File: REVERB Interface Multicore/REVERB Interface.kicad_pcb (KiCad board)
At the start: 2 copper layers, 90.2 x 95.9 mm, 59 parts, among them J1 RPiZeroW, J2 Iridium, J3 APRS, J4 Antenna, J5 UPDI, M1 MountingHole_Pad, M2 MountingHole_Pad, M3 MountingHole_Pad, M4 MountingHole_Pad, M5 PiMount, M6 PiMount, M7 PiMount, M8 PiMount, U1 LSM9DS1BOB, U2 MAX3232, U3 ATtiny1604-SS, U4 TXB0104D

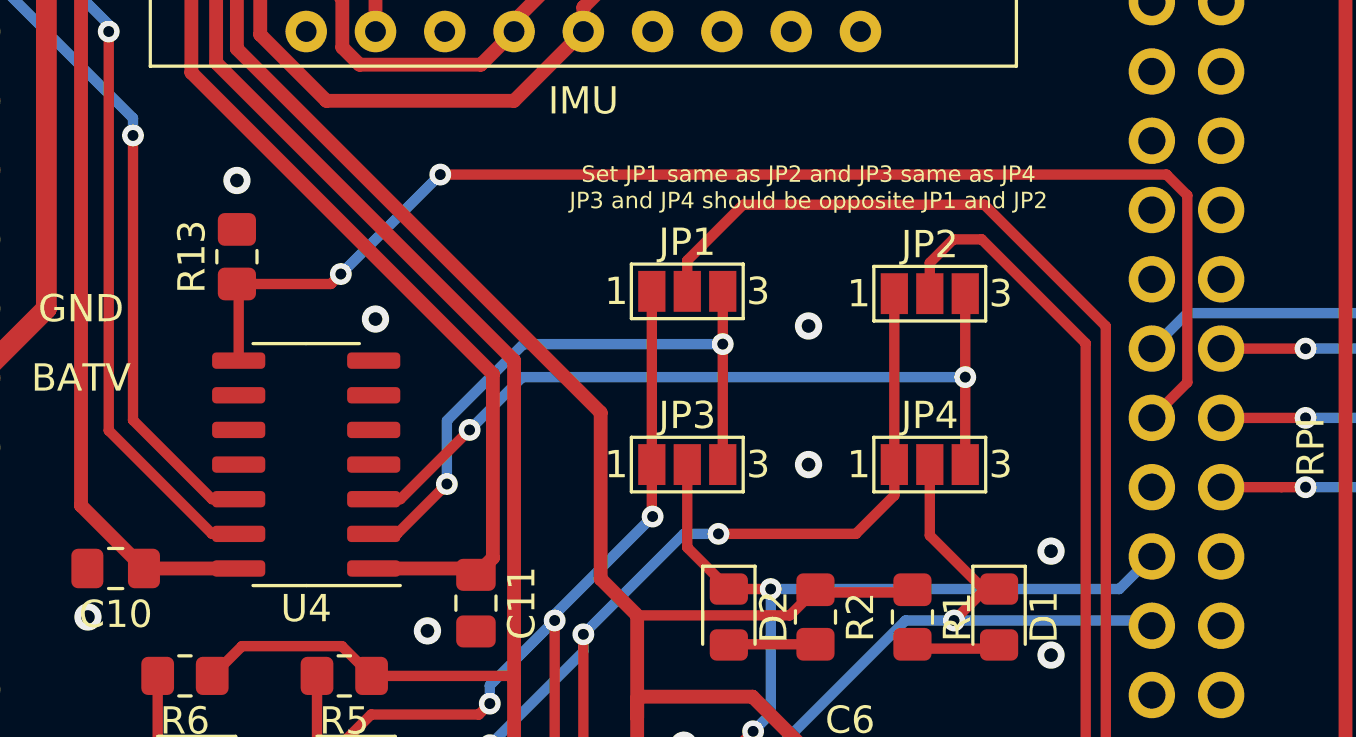
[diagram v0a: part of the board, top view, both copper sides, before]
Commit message: tie OE high
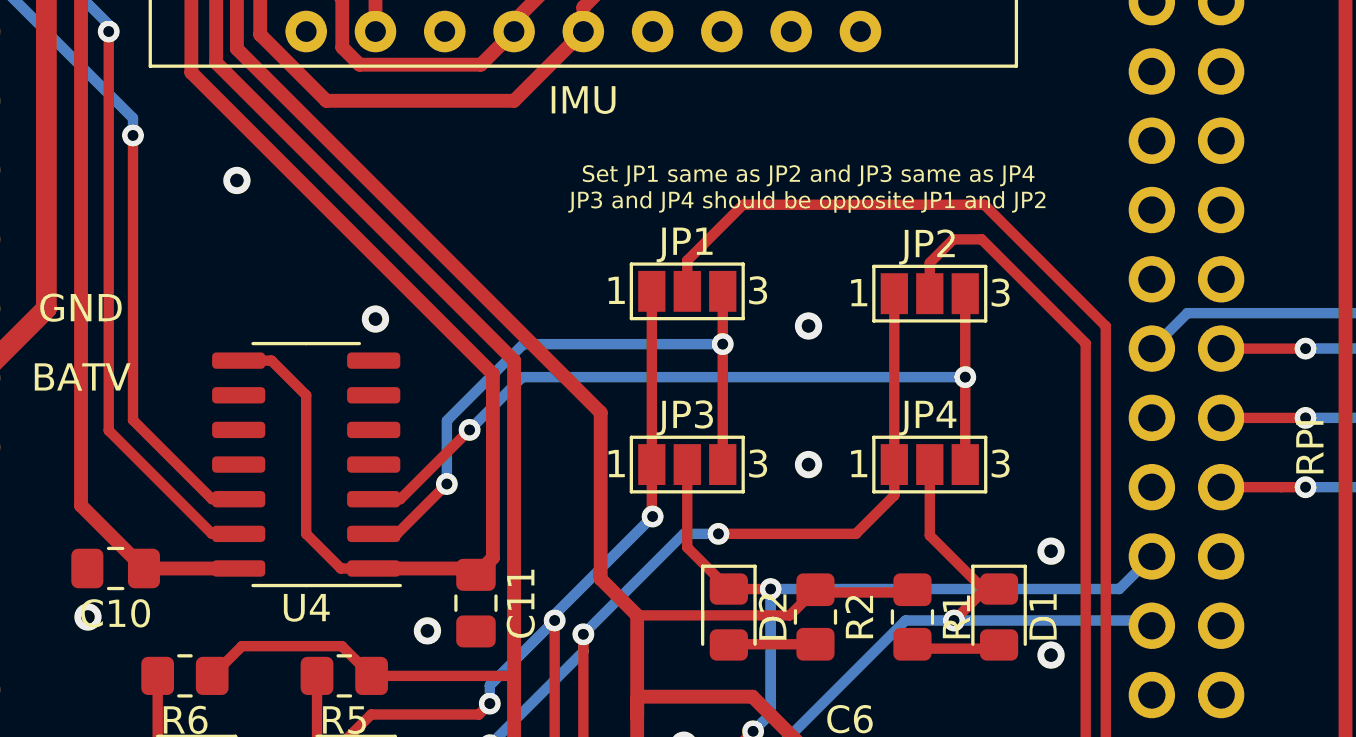
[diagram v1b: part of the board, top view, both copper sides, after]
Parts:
- removed R13: 10K, Resistor_SMD:R_0805_2012Metric_Pad1.20x1.40mm_HandSolder
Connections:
- J1 pad 22: /OE -> (no net)
- U4 pad 8: /OE -> +3V3
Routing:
- net /OE: track 48.3 -> 0.00 mm, vias 2 -> 0
- net +3V3: track 83.4 -> 94.5 mm

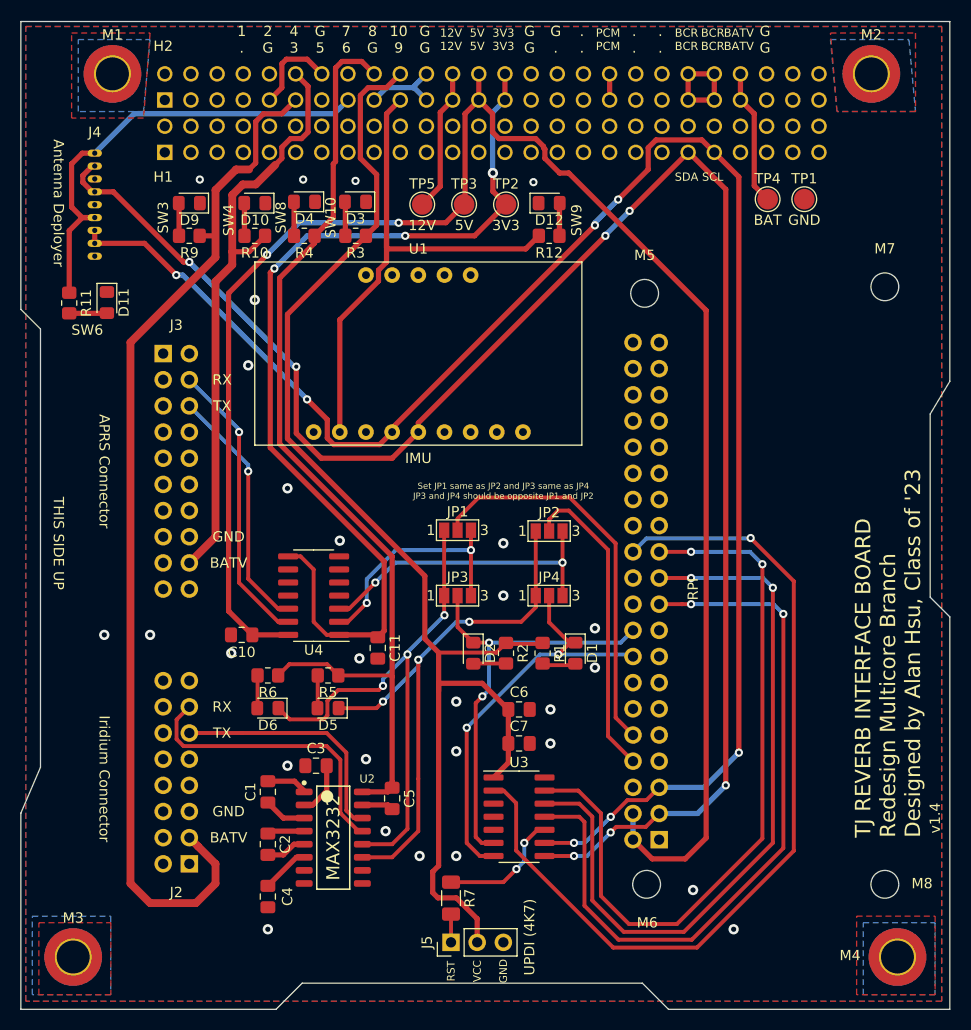
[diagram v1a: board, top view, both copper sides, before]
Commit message: Add decoupling
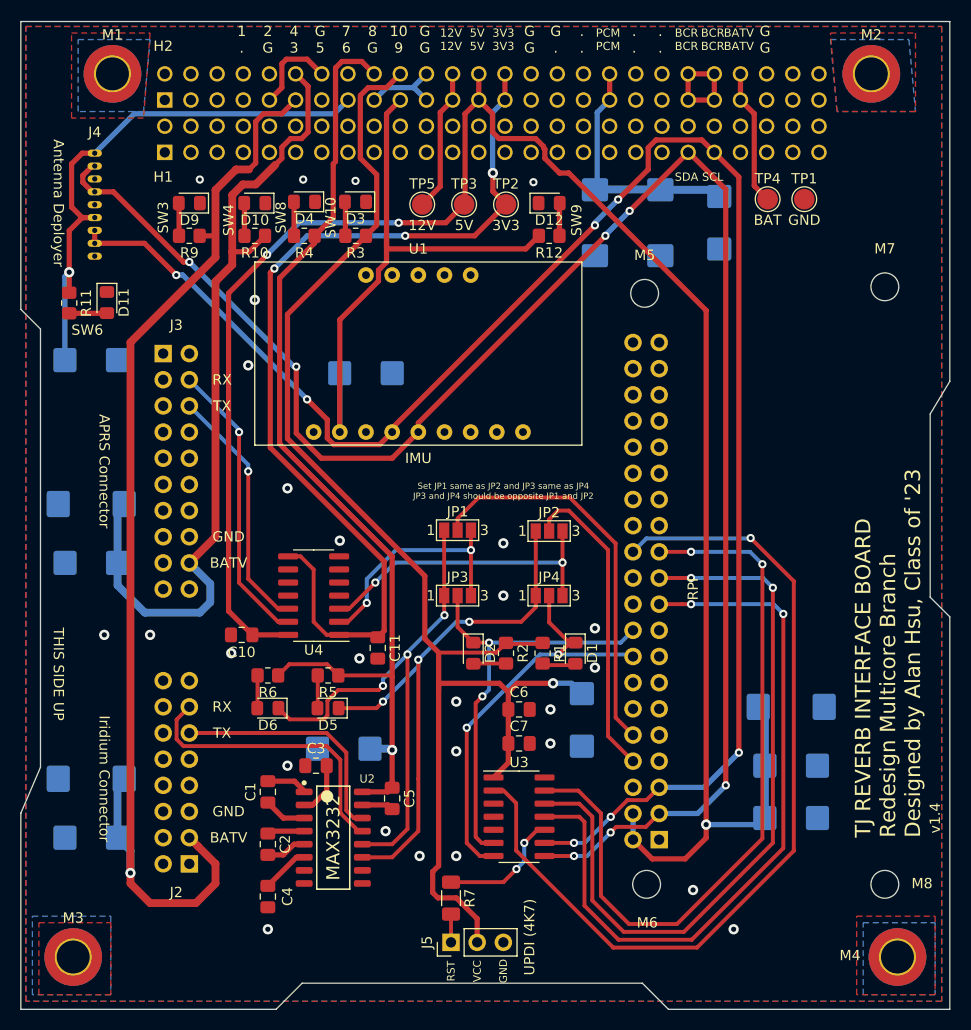
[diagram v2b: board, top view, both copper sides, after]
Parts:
- added C12: 22uF, Capacitor_Tantalum_SMD:CP_EIA-6032-28_Kemet-C_Pad2.25x2.35mm_HandSolder, B.Cu at (181.6, 130.2)
- added C13: 100uF, Capacitor_Tantalum_SMD:CP_EIA-7343-43_Kemet-X_Pad2.25x2.55mm_HandSolder, B.Cu at (113.7, 126.4)
- added C14: 47uF, Capacitor_Tantalum_SMD:CP_EIA-6032-28_Kemet-C_Pad2.25x2.35mm_HandSolder, B.Cu at (113.7, 132.1)
- added C15: 47uF, Capacitor_Tantalum_SMD:CP_EIA-6032-28_Kemet-C_Pad2.25x2.35mm_HandSolder, B.Cu at (113.7, 85.7)
- added C16: 47uF, Capacitor_Tantalum_SMD:CP_EIA-6032-28_Kemet-C_Pad2.25x2.35mm_HandSolder, B.Cu at (140.3, 87.0)
- added C17: 100uF, Capacitor_Tantalum_SMD:CP_EIA-7343-43_Kemet-X_Pad2.25x2.55mm_HandSolder, B.Cu at (162.6, 72.4)
- added C18: 100uF, Capacitor_Tantalum_SMD:CP_EIA-7343-43_Kemet-X_Pad2.25x2.55mm_HandSolder, B.Cu at (168.9, 72.4)
- added C19: 47uF, Capacitor_Tantalum_SMD:CP_EIA-6032-28_Kemet-C_Pad2.25x2.35mm_HandSolder, B.Cu at (174.6, 72.4)
- added C20: 100uF, Capacitor_Tantalum_SMD:CP_EIA-7343-43_Kemet-X_Pad2.25x2.55mm_HandSolder, B.Cu at (113.7, 99.7)
- added C21: 47uF, Capacitor_Tantalum_SMD:CP_EIA-6032-28_Kemet-C_Pad2.25x2.35mm_HandSolder, B.Cu at (113.7, 105.4)
- added C22: 47uF, Capacitor_Tantalum_SMD:CP_EIA-6032-28_Kemet-C_Pad2.25x2.35mm_HandSolder, B.Cu at (138.2, 123.4)
- added C23: 47uF, Capacitor_Tantalum_SMD:CP_EIA-6032-28_Kemet-C_Pad2.25x2.35mm_HandSolder, B.Cu at (161.3, 120.7)
- added C8: 100uF, Capacitor_Tantalum_SMD:CP_EIA-7343-43_Kemet-X_Pad2.25x2.55mm_HandSolder, B.Cu at (181.6, 119.4)
- added C9: 47uF, Capacitor_Tantalum_SMD:CP_EIA-6032-28_Kemet-C_Pad2.25x2.35mm_HandSolder, B.Cu at (181.6, 125.1)
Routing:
- net /SW4: track 57.9 -> 81.3 mm
- net /PCM_IN: track 2.54 -> 24.2 mm
- net +5V: track 171.9 -> 189.0 mm, vias 2 -> 3
- net /SW3: track 101.3 -> 111.3 mm, vias 0 -> 1
- net /SW10: track 126.7 -> 135.6 mm, vias 0 -> 1
- net /SW6: track 45.3 -> 54.0 mm, vias 0 -> 1
- net /SW9: track 51.2 -> 56.9 mm
- net /SW8: track 96.3 -> 98.5 mm, vias 0 -> 1
- net GND: vias 28 -> 27

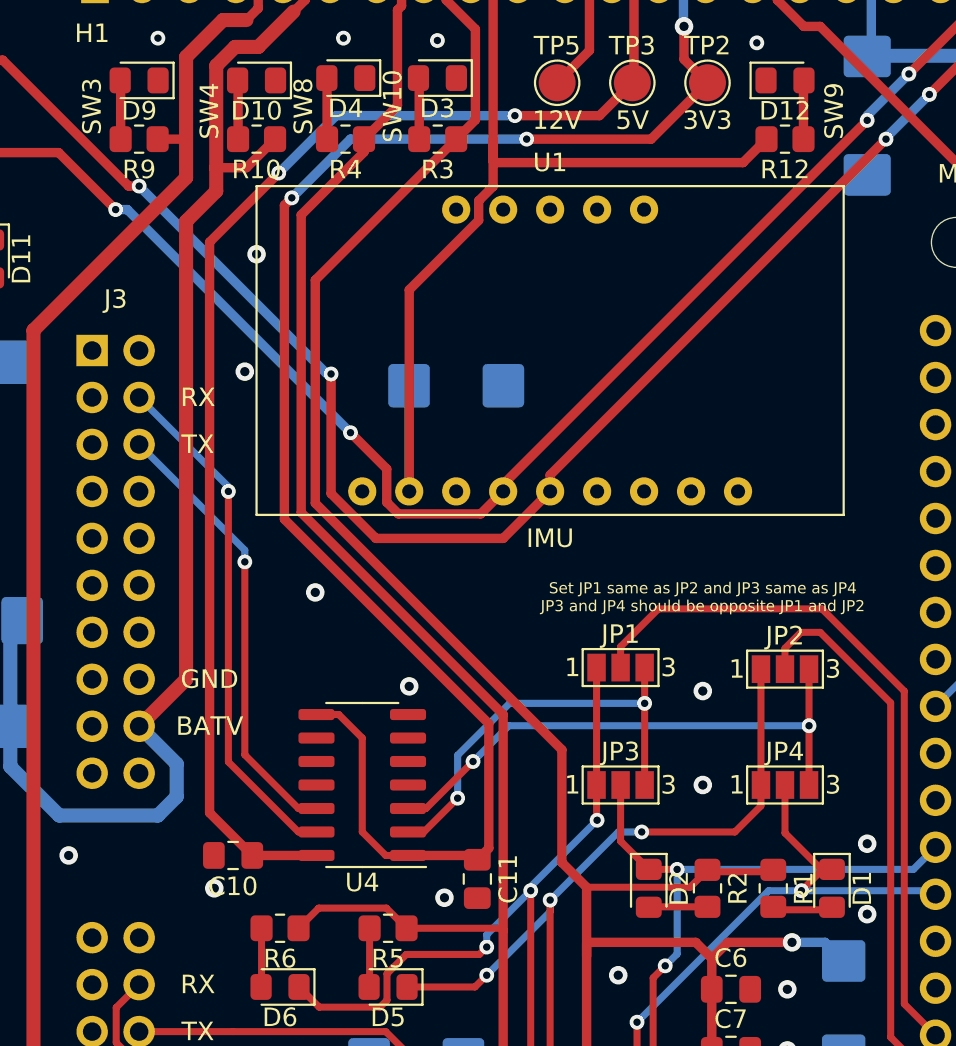
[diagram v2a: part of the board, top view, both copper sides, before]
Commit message: fix imu implementation on multicore branch
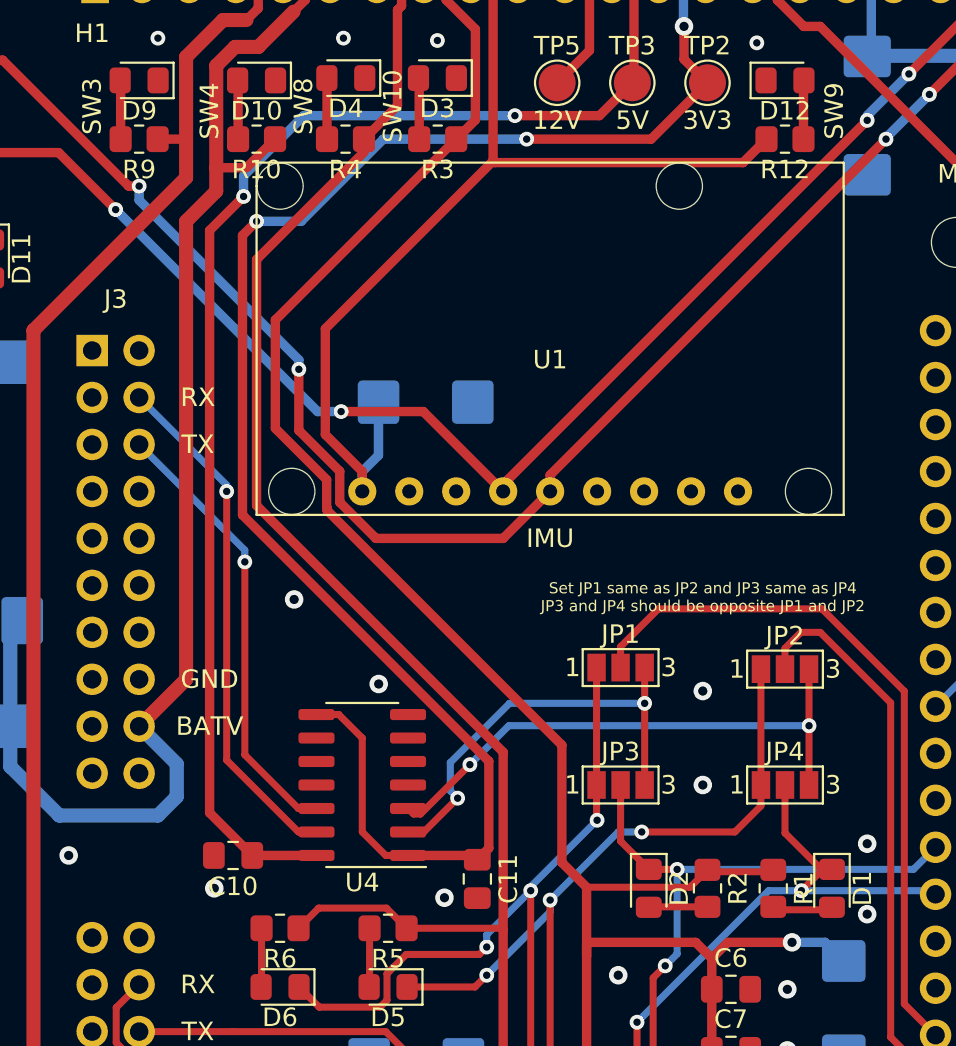
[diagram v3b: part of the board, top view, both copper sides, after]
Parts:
- U1: value LSM9DS1BOB -> IMU; footprint REVERB Interface:LSM9DS1BOB -> REVERB Interface:LSM9DS1-BNO055
- moved C16 1.88 mm to (138.7, 87.9)
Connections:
- U1 pad 1: (no net) -> /SW9
- U1 pad 3: (no net) -> GND
- U1 pad 4: (no net) -> /EPSSCL
- U1 pad 5: (no net) -> /EPSSDA
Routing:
- net +3V3: track 94.5 -> 96.7 mm
- net /EPSSCL: track 166.6 -> 164.6 mm
- net /SW8: track 98.5 -> 100.5 mm
- net /SW10: track 135.6 -> 137.4 mm
- net /SW9: track 56.9 -> 57.9 mm
- net +5V: track 189.0 -> 190.0 mm
- net GND: vias 27 -> 25

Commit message: intermediate commit
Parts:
- U1: footprint REVERB Interface:LSM9DS1-BNO055 -> REVERB Interface:BNO055
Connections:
- J1 pad 32: (no net) -> /IMURST
- U1 pad 4: /EPSSCL -> /EPSSDA
- U1 pad 5: /EPSSDA -> /EPSSCL
- U1 pad 6: (no net) -> /IMURST

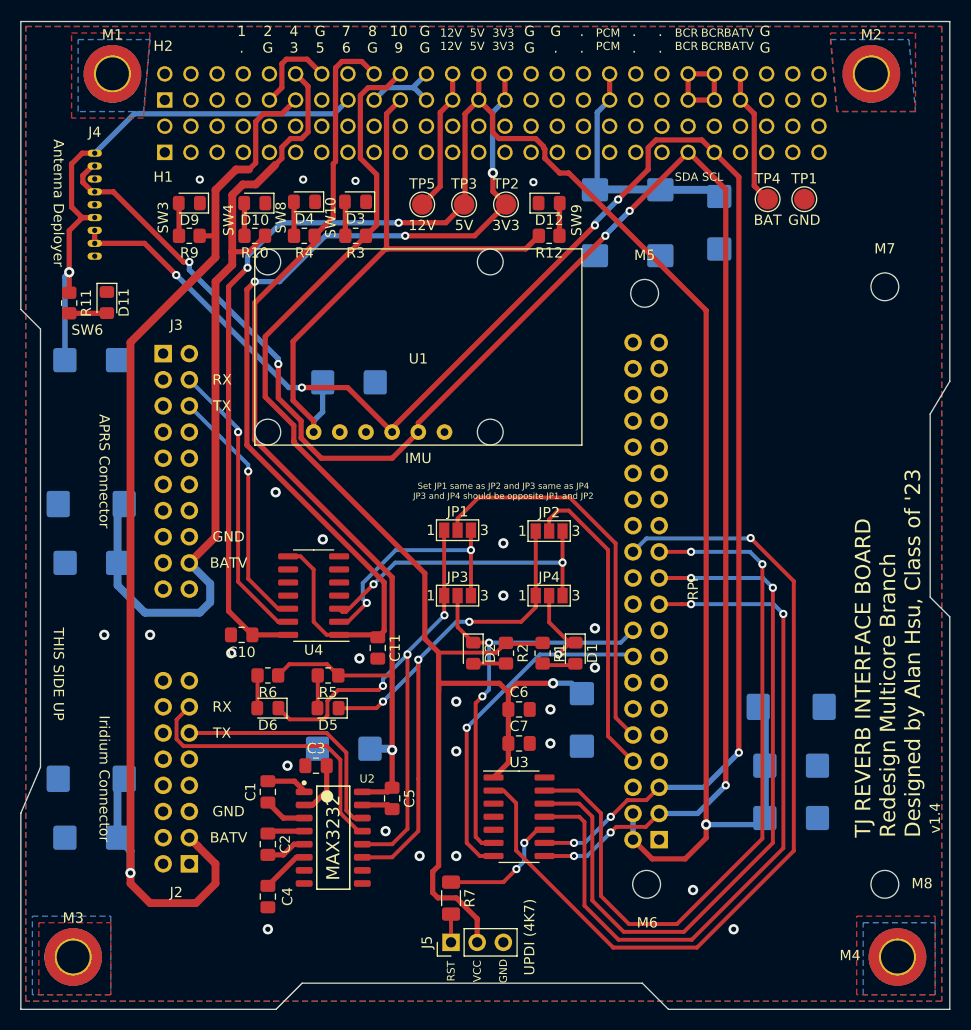
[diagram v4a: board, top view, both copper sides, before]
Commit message: finish bno055 mod, push v1.5
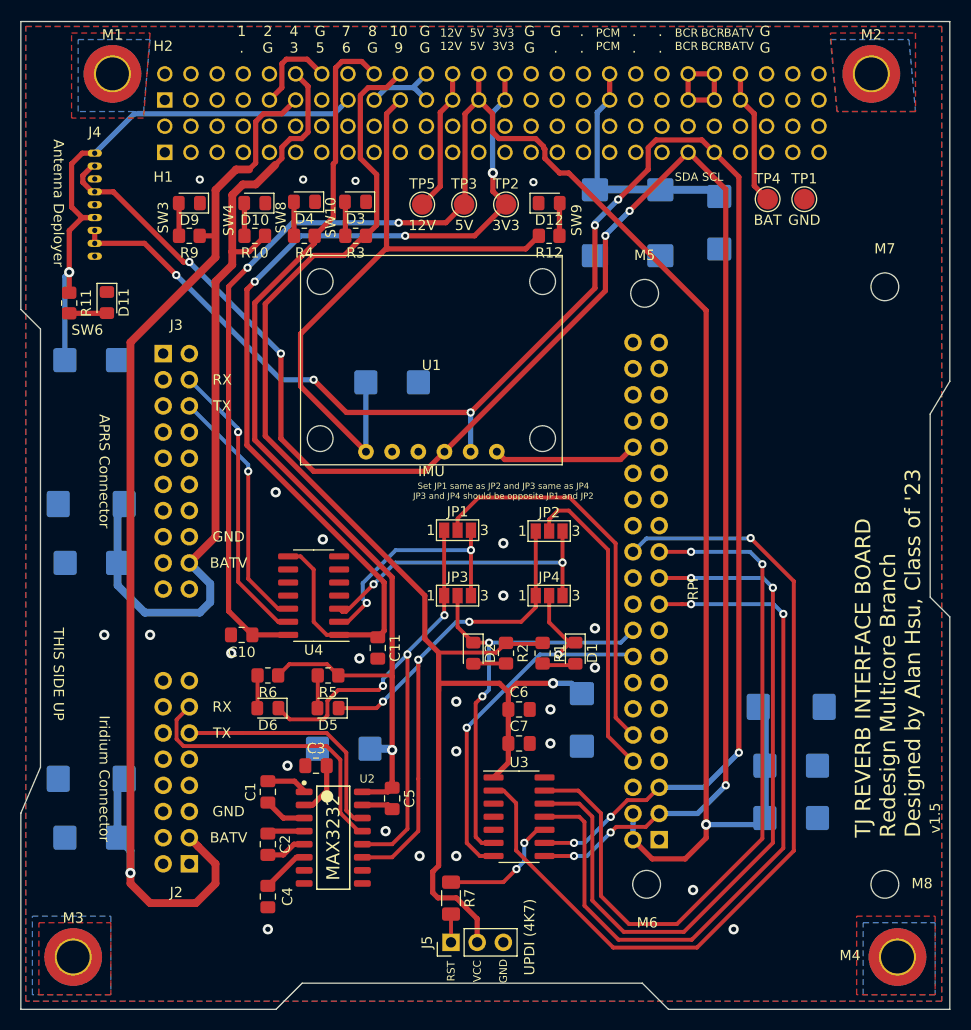
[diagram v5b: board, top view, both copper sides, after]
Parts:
- moved C16 4.19 mm to (142.9, 87.9)
- moved U1 1.42 mm to (146.7, 85.7)
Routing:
- net /IMURST: track 0.00 -> 14.0 mm
- net /EPSSCL: track 164.6 -> 170.2 mm, vias 7 -> 8
- net /SW9: track 57.9 -> 62.9 mm
- net /EPSSDA: track 172.0 -> 176.8 mm
- net /SW10: track 137.4 -> 139.2 mm
- net +5V: track 190.0 -> 189.3 mm
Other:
- board text added: "v1.5"
- board text removed: "v1.4"
